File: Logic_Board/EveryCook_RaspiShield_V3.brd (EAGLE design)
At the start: 103.1 x 86.4 mm, 94 parts, among them IC1 LM386MM-1, IC2 ATMEGA644A, Q1 8 MHz, Q2 BSP372, Q3 BSP372, T2 ZDT6790, U1 AD7794BRUZ, U4 78M05, U7 CJ1117-3.3

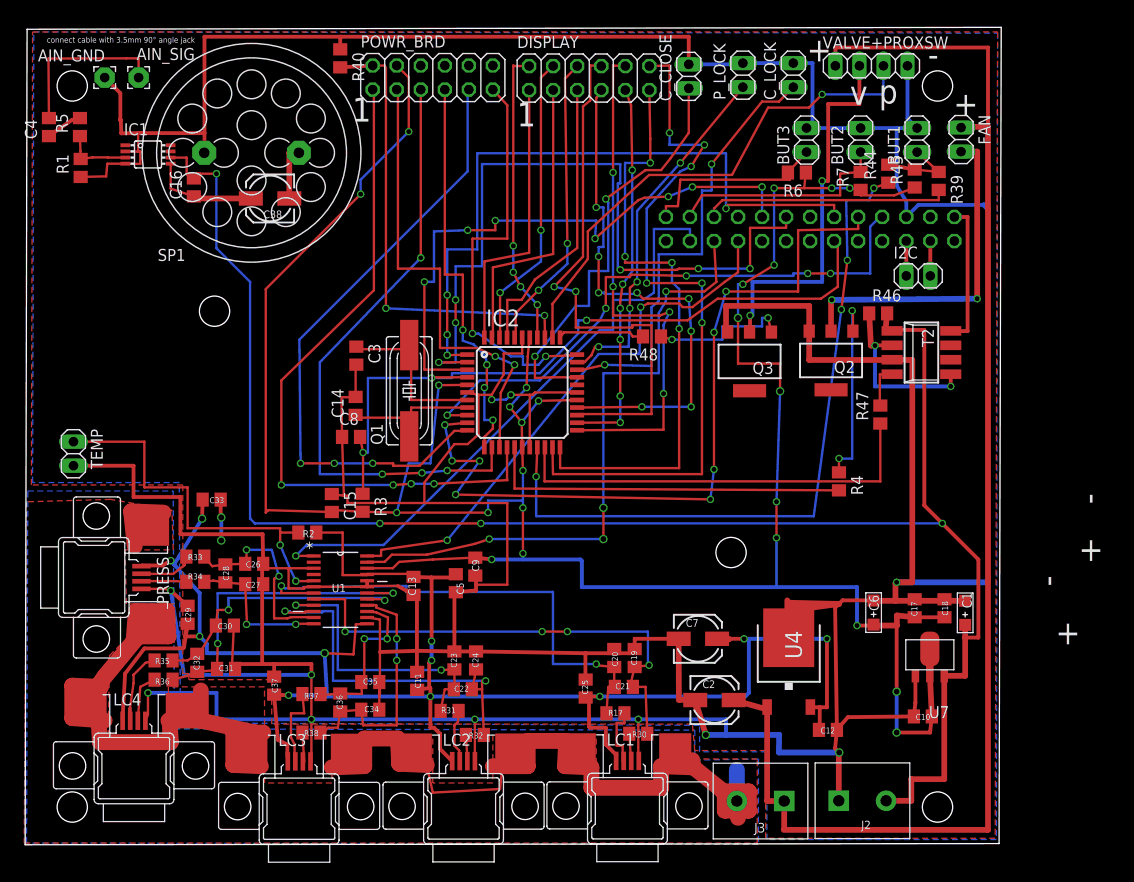
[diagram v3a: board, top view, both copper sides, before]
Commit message: Cleaned up the logic board. added safety chain board.
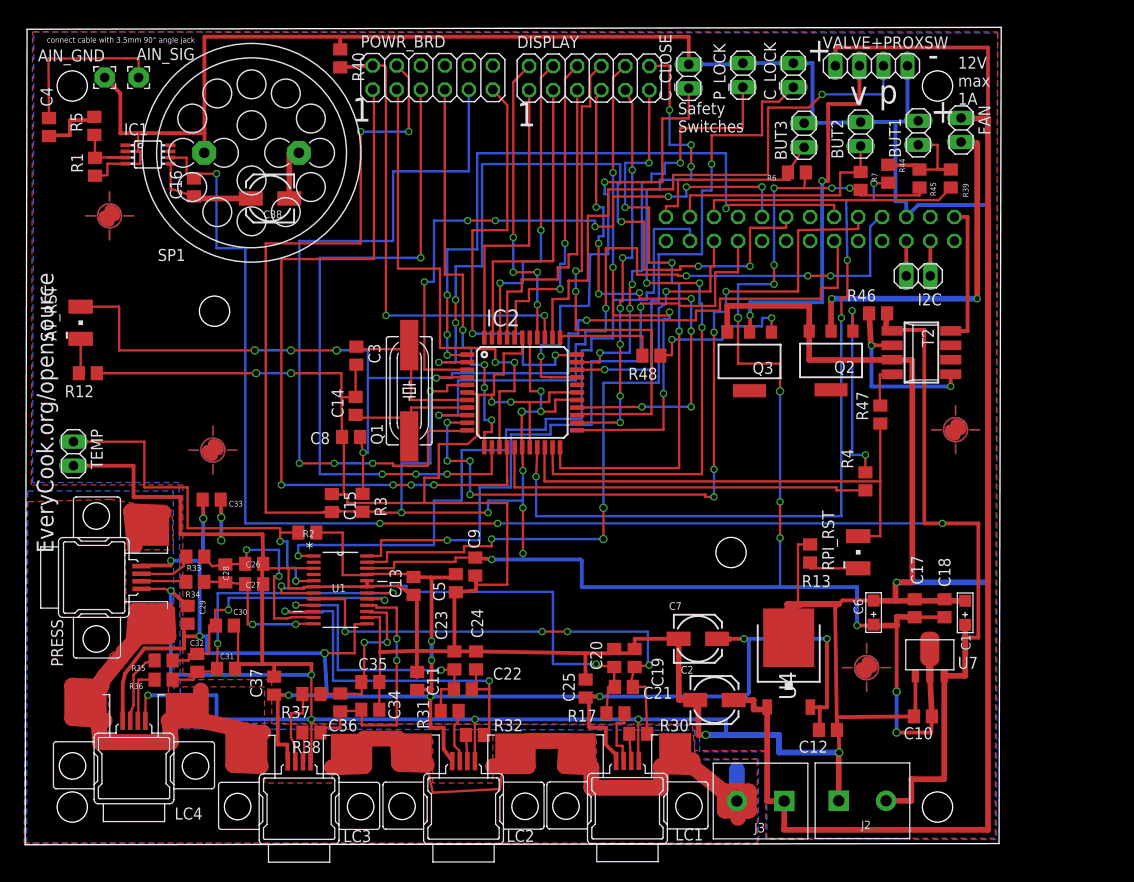
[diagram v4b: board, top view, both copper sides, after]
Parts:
- added AT_RST, RPI_RST: LG_T679-E1F1-1, led:PLCC2
- added R12, R13: 100, rcl:R0805
- added U$1, U$2, U$3, U$4: (no value), marks:PASS-ROUND
- C8: value 100nF -> 0.1uF
- moved R4 2.79 mm to (88.9, 34.4)
- moved R48 2.03 mm to (66.3, 47.7)
- moved R1 1.53 mm to (7.49, 67.7)
- moved R5 1.53 mm to (7.42, 72.0)
- moved R39 1.30 mm to (97.9, 66.4)
- moved FAN 1.02 mm to (99.0, 71.6)
- moved BUT1 0.77 mm to (94.5, 71.2)
- moved BUT2 0.64 mm to (88.4, 71.1)
- moved BUT3 0.57 mm to (82.4, 71.0)
- moved R45 0.51 mm to (94.6, 66.4)
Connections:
- removed net N$6: C8.2, IC2.4, R3.1, RASPI_CONNECTOR_(TOP).11
- new net ATMEL_RST: AT_RST.A, C8.2, IC2.4, R3.1, RASPI_CONNECTOR_(TOP).11
- new net N$32: AT_RST.C, R12.2
- new net N$34: R13.2, RPI_RST.C
- net GND: now also R12.1, R13.1
- net RPI_RST: now also RPI_RST.A
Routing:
- net ATMEL_RST: track 0.00 -> 120.2 mm, vias 0 -> 6
- net N$6: track 78.0 -> 0.00 mm, vias 3 -> 0
- net GND: track 718.0 -> 757.7 mm, vias 13 -> 15
- net +3V3: track 290.1 -> 304.4 mm, vias 25 -> 24
- net MOSI: track 58.9 -> 73.0 mm
- net SCLK: track 64.8 -> 78.9 mm
- net N$52: track 62.2 -> 76.1 mm
- net IH_OFF: track 66.4 -> 79.1 mm
- net PROX_SWI: track 53.9 -> 62.8 mm
- net N$61: track 38.3 -> 46.4 mm
- net RPI_RST: track 45.2 -> 53.4 mm
- net IH_ON: track 65.7 -> 72.3 mm
- net IH_PWR: track 73.3 -> 79.5 mm
- net +5V: track 187.5 -> 193.3 mm
- net N$59: track 44.9 -> 50.6 mm
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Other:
- board text added: "12V max 1A"
- board text added: "Safety Switches"
- board text added: "user input"
- board text removed: "+Motor-"
- board text removed: "- DC +"
- board text removed: "7-seg LED"
- board text removed: "LOADCELL 1 & 2"
- board text removed: "LOADCELL 3 & 4"
- board text removed: "M+ PG"
- board text removed: "Motor"
- board text removed: "Press & servo"
- board text removed: "Temp & Button"

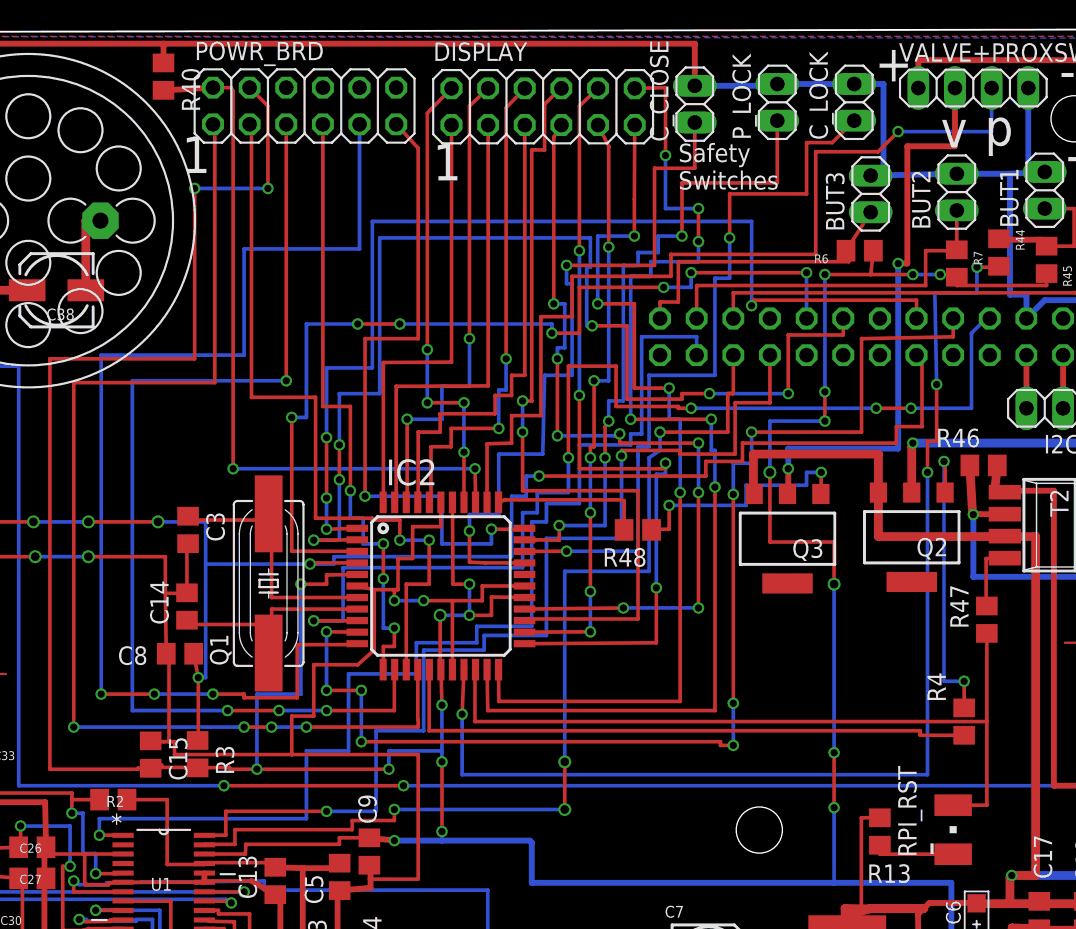
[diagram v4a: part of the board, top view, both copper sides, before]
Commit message: Re-routed a display pin to have the whole display on ports B and C. Safety chain board layouted.
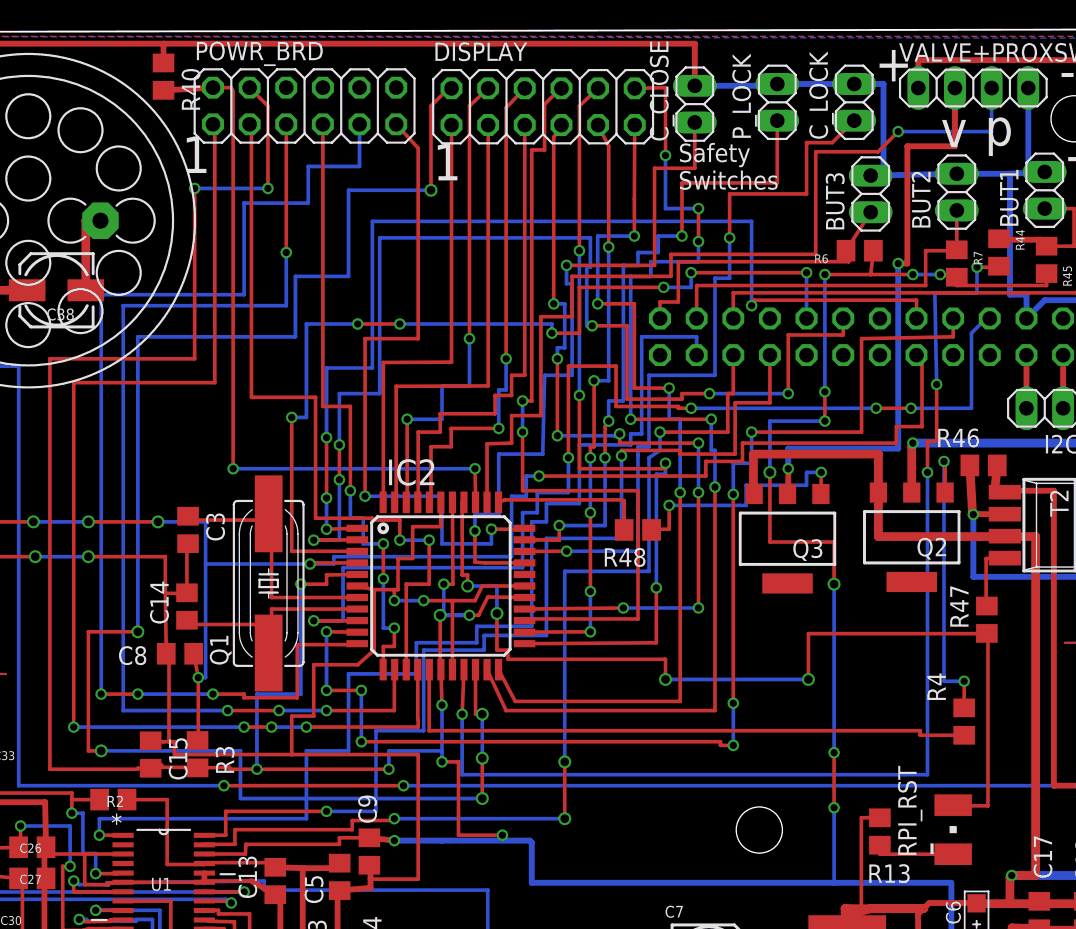
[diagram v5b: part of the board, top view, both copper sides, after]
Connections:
- removed net N$49: DISPLAY.2, IC2.37
- new net N$1: DISPLAY.2, IC2.20
- net RPI_RST: now also IC2.37; no longer IC2.20
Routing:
- net N$1: track 0.00 -> 110.4 mm, vias 0 -> 6
- net N$49: track 31.9 -> 0.00 mm, vias 4 -> 0
- net RPI_RST: track 53.4 -> 66.5 mm, vias 0 -> 4
- net +3V3: track 304.4 -> 313.6 mm
- net IH_ON: track 72.3 -> 73.6 mm
- net N$11: track 76.7 -> 75.7 mm
- net N$15: track 63.0 -> 62.1 mm
- net N$59: track 50.6 -> 49.8 mm
